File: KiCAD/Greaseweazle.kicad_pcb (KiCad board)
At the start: 2 copper layers, 44.5 x 19 mm, 22 parts, among them J1 USB_B_Micro, J2 PROG, J3 POWER, J4 Conn_02x17_Odd_Even, U1 SPX3819M5-L-3-3, U2 STM32F103C8Tx, Y1 8M

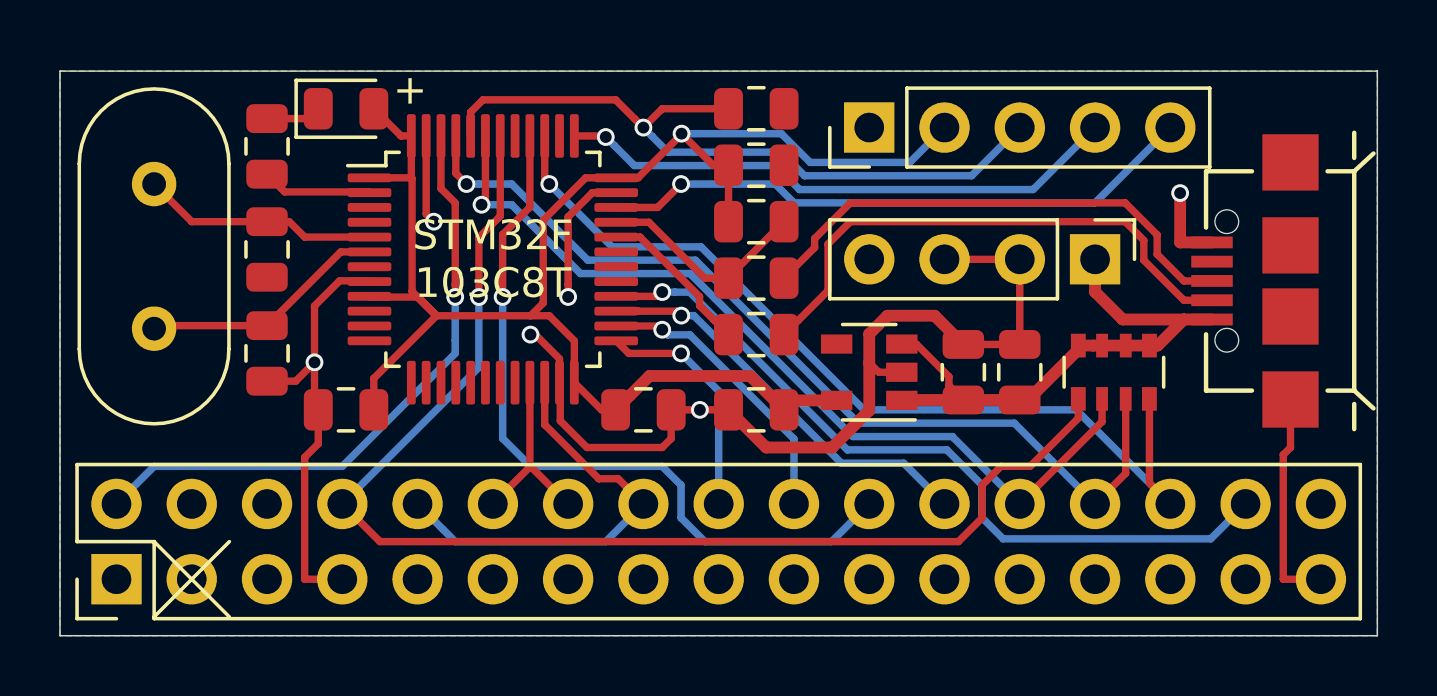
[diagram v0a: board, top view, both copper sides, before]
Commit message: Kicad : 0.2 with additional regulator footprint, DISKCHANGE signal and ID jumpers
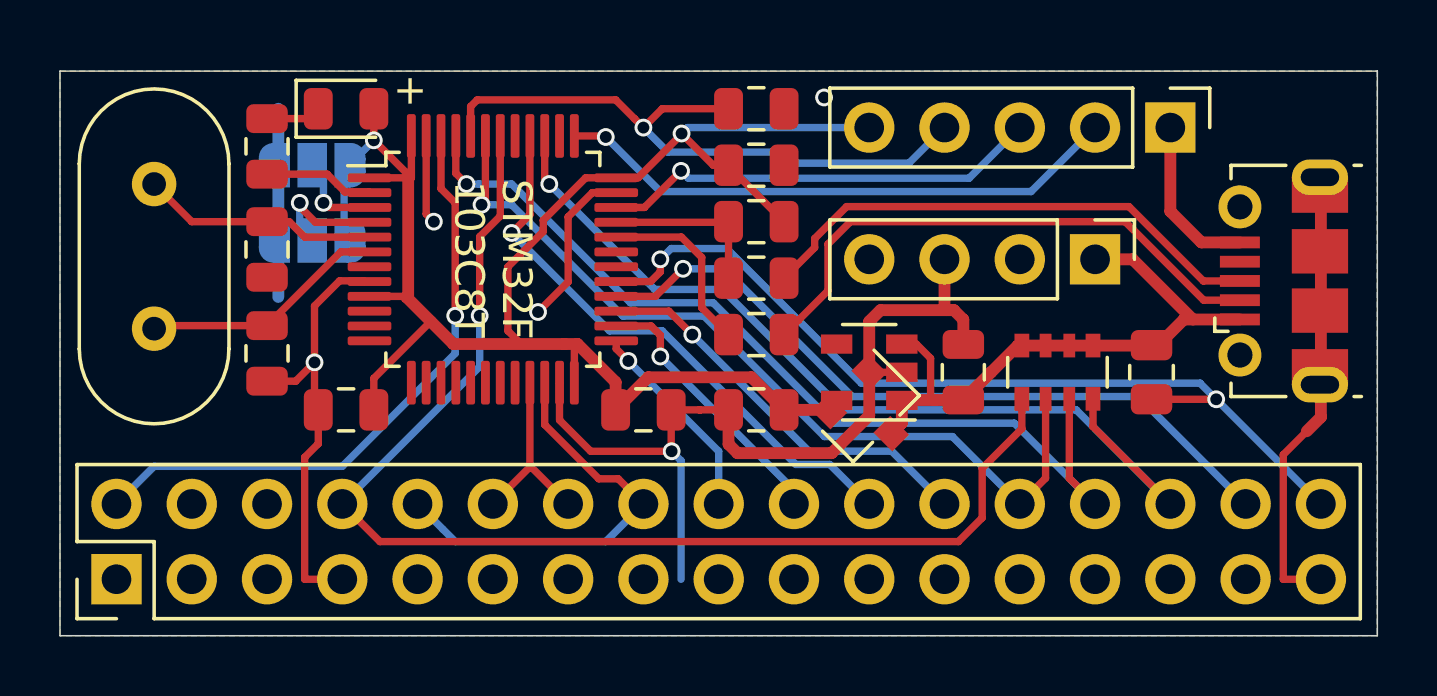
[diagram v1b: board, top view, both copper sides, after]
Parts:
- removed C9: 1u, Capacitor_SMD:C_0805_2012Metric
- added JP1: ID0, Jumper:SolderJumper-3_P1.3mm_Open_RoundedPad1.0x1.5mm, B.Cu at (143.8, 137.8)
- added JP2: ID1, Jumper:SolderJumper-3_P1.3mm_Open_RoundedPad1.0x1.5mm, B.Cu at (143.8, 140.3)
- added R4: 1k, Resistor_SMD:R_0805_2012Metric, F.Cu at (172.1, 144.8)
- added U3: XC6206PxxxMR, Package_TO_SOT_SMD:SOT-23, F.Cu at (162.6, 146.1)
- J1: footprint Sassa:USB-MICRO-B -> Connector_USB:USB_Micro-B_Molex-105017-0001
- moved J2 10.2 mm to (172.7, 136.5), turned to 270 degrees
- moved RN1 1.91 mm to (168.9, 144.8)
- moved J1 0.25 mm to (176.5, 141.7)
- turned R5 to 180 degrees
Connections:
- J2 pad 2: +3V3 -> /SWCLK
- J2 pad 3: /BOOT0 -> /SWDIO
- J2 pad 4: /SWCLK -> /BOOT0
- J2 pad 5: /SWDIO -> +3V3
- J4 pad 34: Net-(J4-Pad34) -> /_DSKCHG
- U2 pad 29: Net-(U2-Pad29) -> /_DSKCHG
- U2 pad 3: Net-(U2-Pad3) -> /ID0
- U2 pad 4: Net-(U2-Pad4) -> /ID1
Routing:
- net /_DSKCHG: track 0.00 -> 30.2 mm, vias 0 -> 2
- net GND: track 64.0 -> 81.1 mm, vias 6 -> 5
- net /_DKWD: track 25.6 -> 19.4 mm
- net /SWDIO: track 20.3 -> 14.9 mm
- net /ID1: track 0.00 -> 4.14 mm, vias 0 -> 1
- net +3V3: track 56.7 -> 60.0 mm, vias 1 -> 2
- net /ID0: track 0.00 -> 3.04 mm, vias 0 -> 1
- net /BOOT0: track 24.4 -> 21.6 mm
- net Net-(R5-Pad2): track 7.25 -> 5.70 mm
- net +5V: track 19.2 -> 20.6 mm
- net /_INDEX: track 43.0 -> 41.6 mm
- net /_DIR: track 7.97 -> 6.94 mm
- net /_SIDE: track 25.9 -> 24.9 mm
- net Net-(R6-Pad2): track 5.33 -> 6.15 mm
- net /_TRK0: track 29.4 -> 28.6 mm
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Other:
- board text added: "1"
- board text added: "ID0"
- board text added: "ID1"
- board text added: "original design by Keir Fraser, adapted by FLACO 2020 v0.2"
- board text removed: "original design by Keir Fraser, adapted by FLACO 2020 v0.1"
